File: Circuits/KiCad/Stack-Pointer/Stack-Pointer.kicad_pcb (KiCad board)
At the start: 2 copper layers, 54.6 x 51.4 mm, 7 parts, among them J1 Conn_01x06_Male, J2 MEMORY ADDRESS, U1 74x02, U2 74x191, U3 74x191

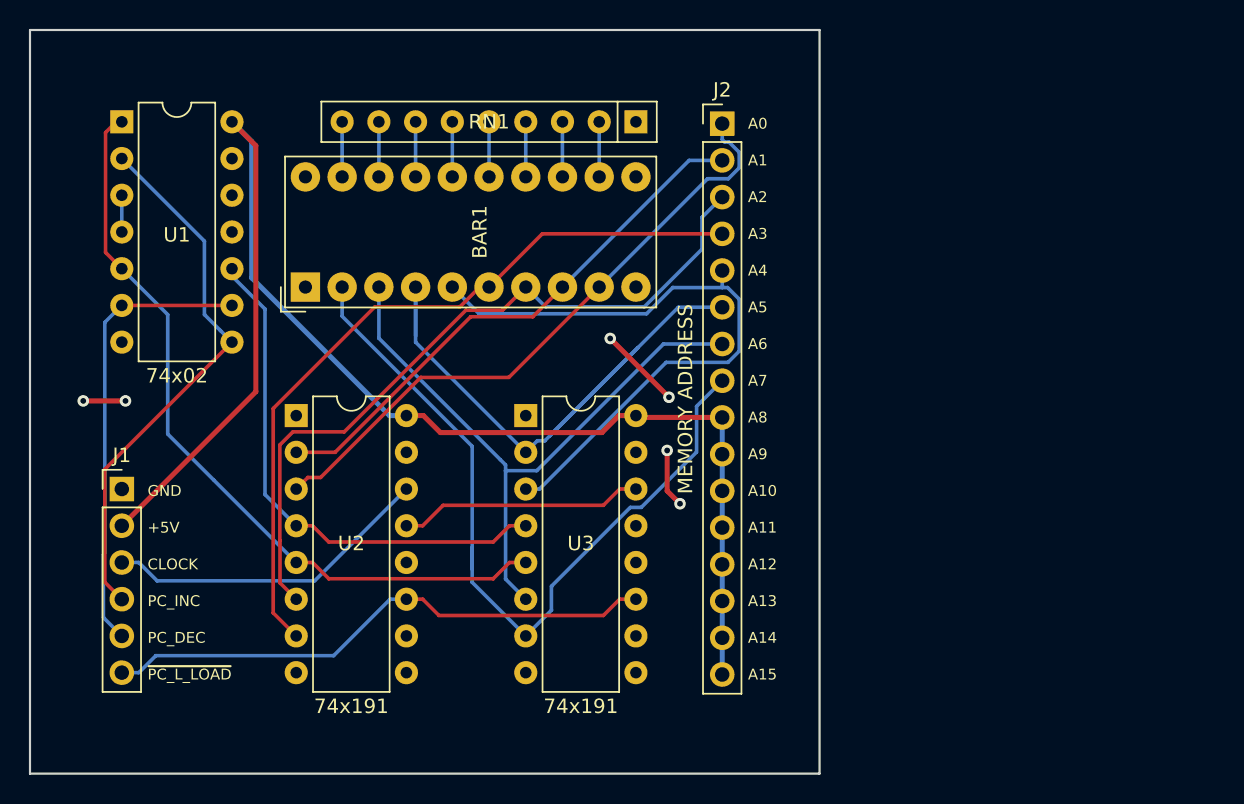
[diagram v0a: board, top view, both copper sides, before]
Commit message: Made sure spacing between headers is always 2.54mm pitch
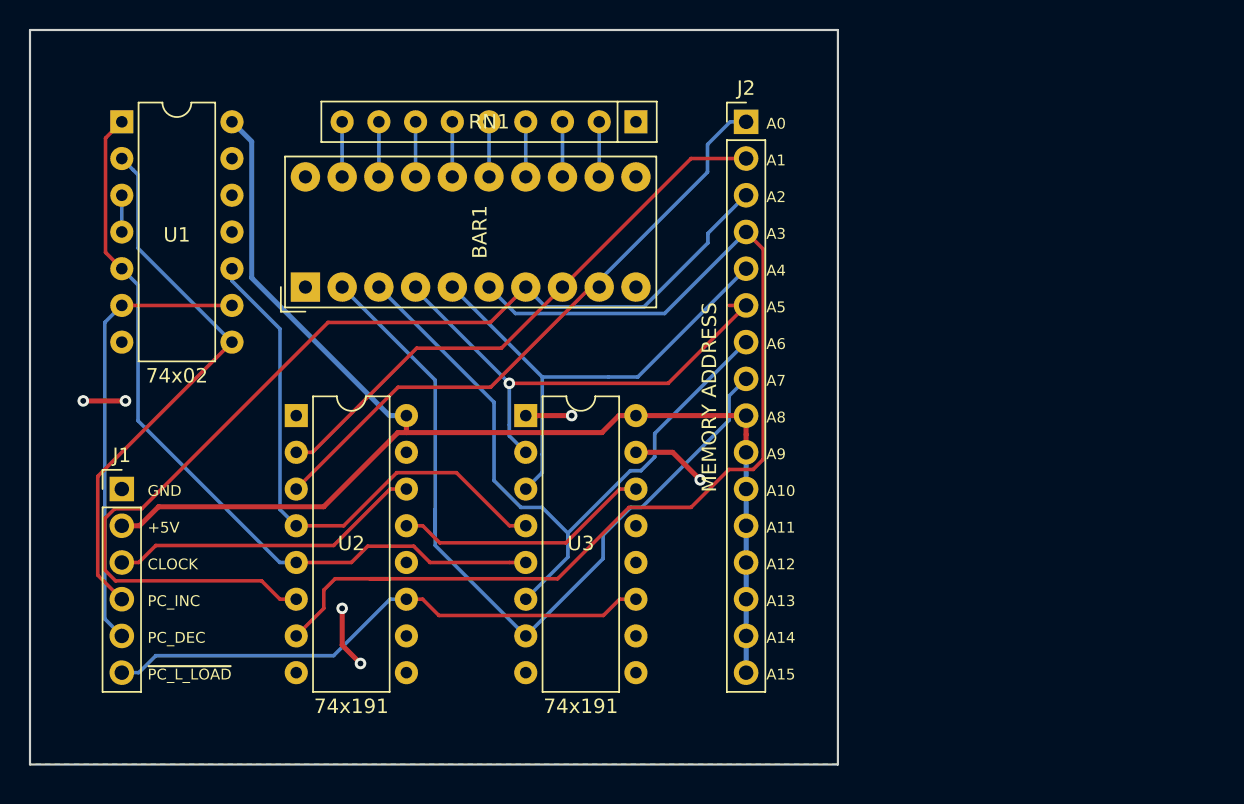
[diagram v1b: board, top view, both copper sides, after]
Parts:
- moved J2 1.66 mm to (97.8, 28.6)
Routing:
- net Net-(BAR1-Pad6): track 52.5 -> 76.5 mm
- net Net-(BAR1-Pad7): track 51.3 -> 72.8 mm
- net Net-(BAR1-Pad5): track 45.2 -> 34.2 mm
- net Net-(BAR1-Pad4): track 44.3 -> 34.4 mm, vias 0 -> 1
- net +5V: track 99.1 -> 91.3 mm
- net Net-(BAR1-Pad3): track 44.4 -> 47.8 mm
- net GND: track 12.7 -> 15.7 mm
- net ~CLK_EN: track 36.4 -> 38.5 mm
- net Net-(BAR1-Pad8): track 37.8 -> 39.5 mm
- net CLOCK: track 22.8 -> 21.8 mm
- net Net-(U2-Pad13): track 16.9 -> 17.9 mm
- net Net-(BAR1-Pad2): track 54.6 -> 55.5 mm
- net Net-(BAR1-Pad9): track 43.6 -> 43.0 mm
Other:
- board size 54.6 x 51.4 mm -> 55.9 x 50.8 mm

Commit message: Updated Stack Pointer schematic and PCB
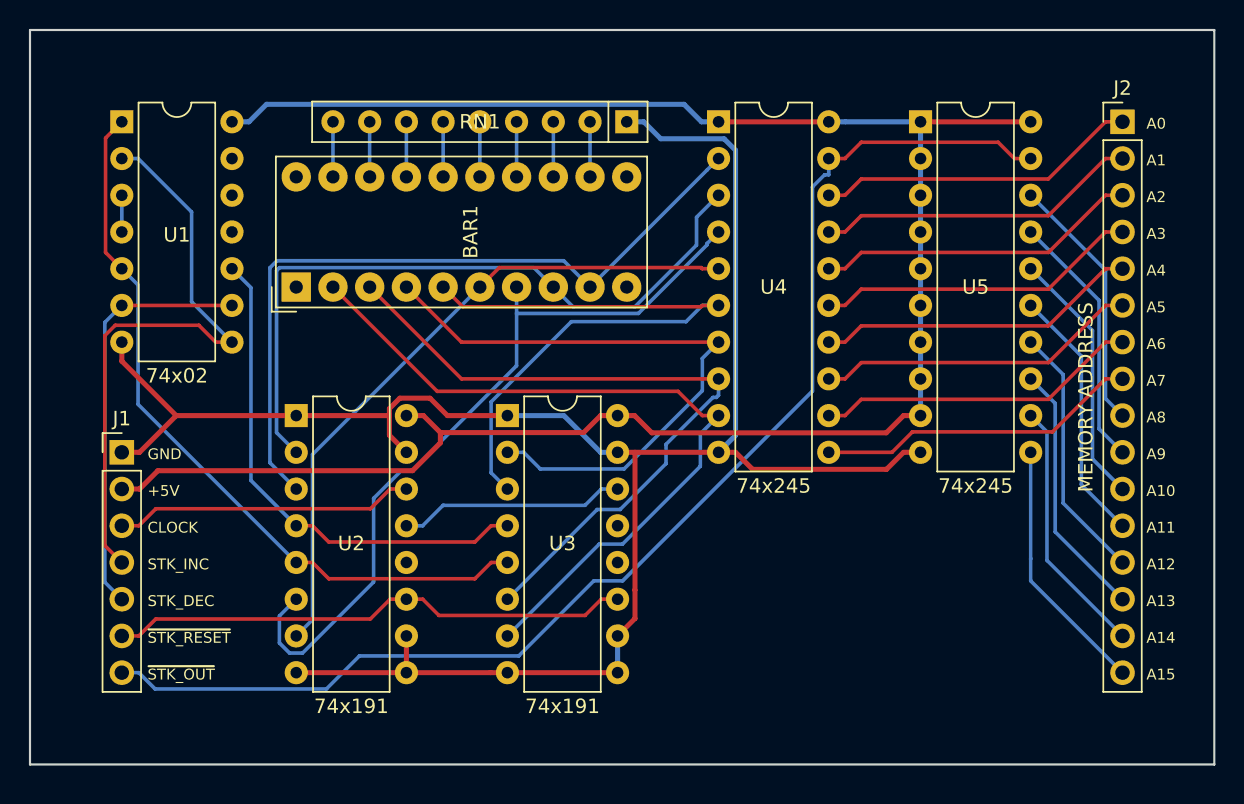
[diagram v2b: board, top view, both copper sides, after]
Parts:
- added U4: 74x245, Package_DIP:DIP-20_W7.62mm, F.Cu at (95.9, 28.6)
- added U5: 74x245, Package_DIP:DIP-20_W7.62mm, F.Cu at (109.9, 28.6)
- J1: value Conn_01x06_Male -> Conn_01x07_Male; footprint Connector_PinHeader_2.54mm:PinHeader_1x06_P2.54mm_Vertical -> Connector_PinHeader_2.54mm:PinHeader_1x07_P2.54mm_Vertical
- moved J2 26.0 mm to (123.8, 28.6)
- moved J1 2.54 mm to (54.6, 51.4)
- moved U3 1.27 mm to (81.3, 48.9)
- moved BAR1 0.64 mm to (66.7, 40.0)
- moved RN1 0.64 mm to (89.5, 28.6)
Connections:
- J2 pad 1: Net-(BAR1-Pad9) -> Net-(J2-Pad1)
- J2 pad 10: +5V -> Net-(J2-Pad10)
- J2 pad 11: +5V -> Net-(J2-Pad11)
- J2 pad 12: +5V -> Net-(J2-Pad12)
- J2 pad 13: +5V -> Net-(J2-Pad13)
- J2 pad 14: +5V -> Net-(J2-Pad14)
- J2 pad 15: +5V -> Net-(J2-Pad15)
- J2 pad 16: +5V -> Net-(J2-Pad16)
- J2 pad 2: Net-(BAR1-Pad8) -> Net-(J2-Pad2)
- J2 pad 3: Net-(BAR1-Pad7) -> Net-(J2-Pad3)
- J2 pad 4: Net-(BAR1-Pad6) -> Net-(J2-Pad4)
- J2 pad 5: Net-(BAR1-Pad5) -> Net-(J2-Pad5)
- J2 pad 6: Net-(BAR1-Pad4) -> Net-(J2-Pad6)
- J2 pad 7: Net-(BAR1-Pad3) -> Net-(J2-Pad7)
- J2 pad 8: Net-(BAR1-Pad2) -> Net-(J2-Pad8)
- J2 pad 9: +5V -> Net-(J2-Pad9)
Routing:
- net GND: track 15.7 -> 139.5 mm, vias 6 -> 0
- net ~STK_OUT: track 0.00 -> 88.4 mm
- net +5V: track 91.3 -> 138.2 mm
- net Net-(BAR1-Pad6): track 76.5 -> 46.5 mm
- net Net-(J2-Pad8): track 0.00 -> 22.4 mm
- net Net-(J2-Pad7): track 0.00 -> 22.4 mm
- net Net-(J2-Pad6): track 0.00 -> 22.4 mm
- net Net-(J2-Pad5): track 0.00 -> 22.4 mm
- net Net-(J2-Pad4): track 0.00 -> 22.4 mm
- net Net-(J2-Pad2): track 0.00 -> 22.4 mm
- net Net-(J2-Pad1): track 0.00 -> 22.4 mm
- net Net-(J2-Pad3): track 0.00 -> 22.4 mm
- net Net-(BAR1-Pad7): track 72.8 -> 53.6 mm
- net Net-(J2-Pad9): track 0.00 -> 17.9 mm
- net Net-(J2-Pad15): track 0.00 -> 17.9 mm
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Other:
- board size 55.9 x 50.8 mm -> 81.9 x 50.8 mm
- board text added: "STK_DEC"
- board text added: "STK_INC"
- board text added: "~STK_OUT"
- board text added: "~STK_RESET"
- board text removed: "PC_DEC"
- board text removed: "PC_INC"
- board text removed: "~PC_L_LOAD"

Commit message: Updated pin header row pitch
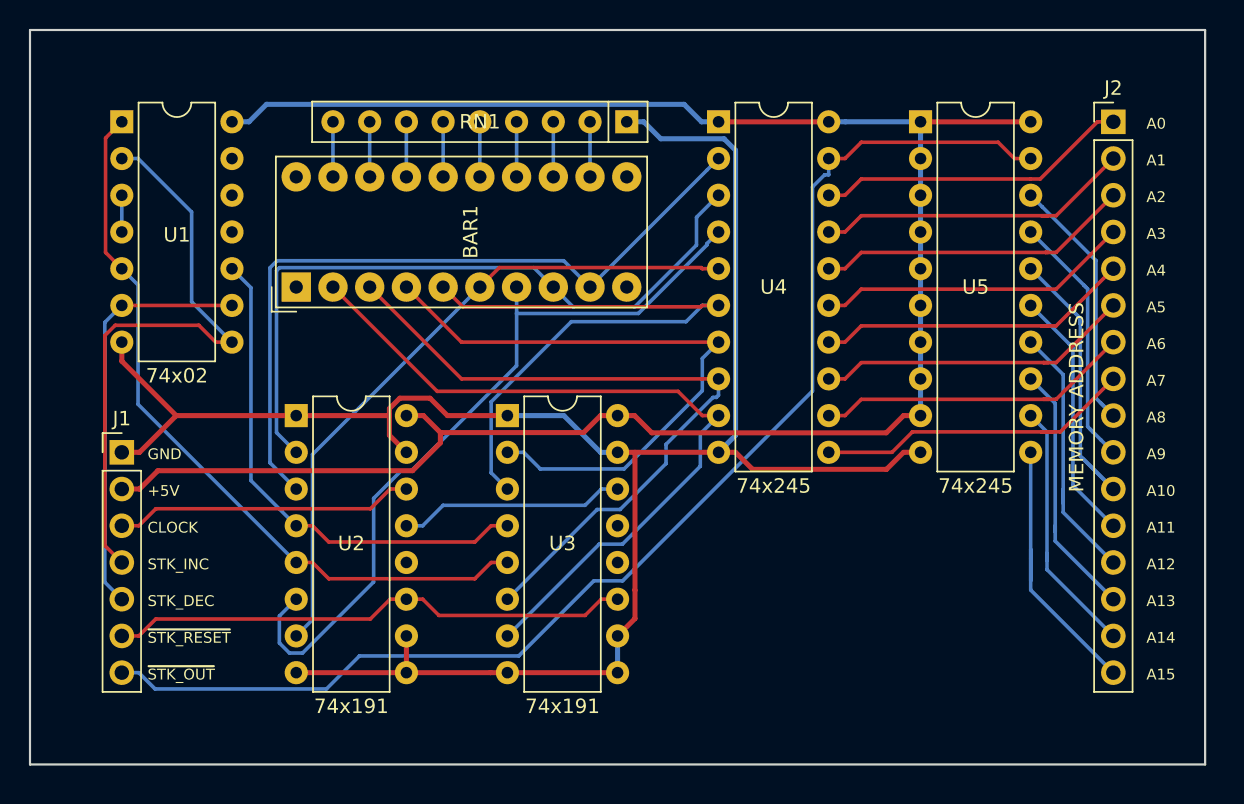
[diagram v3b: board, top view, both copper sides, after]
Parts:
- moved J2 0.64 mm to (123.2, 28.6)
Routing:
- net Net-(J2-Pad11): track 17.9 -> 20.9 mm
- net Net-(J2-Pad16): track 17.9 -> 19.8 mm
- net Net-(J2-Pad8): track 22.4 -> 23.7 mm
- net Net-(J2-Pad2): track 22.4 -> 23.4 mm
- net Net-(J2-Pad5): track 22.4 -> 23.4 mm
- net Net-(J2-Pad9): track 17.9 -> 18.9 mm
- net Net-(J2-Pad7): track 22.4 -> 23.3 mm
- net Net-(J2-Pad6): track 22.4 -> 23.3 mm
- net Net-(J2-Pad3): track 22.4 -> 23.2 mm
- net Net-(J2-Pad13): track 17.9 -> 18.6 mm
- net Net-(J2-Pad4): track 22.4 -> 23.0 mm
- net Net-(J2-Pad1): track 22.4 -> 23.0 mm
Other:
- board size 81.9 x 50.8 mm -> 81.3 x 50.8 mm
